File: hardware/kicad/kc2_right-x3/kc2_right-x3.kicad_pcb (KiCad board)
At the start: 2 copper layers, 194.8 x 133.8 mm, 98 parts, among them SW1 KEY_01, SW10 KEY_10, SW11 KEY_11, SW12 KEY_12, SW13 KEY_13, SW14 KEY_14, SW15 KEY_15, SW16 KEY_16, SW17 KEY_17, SW18 KEY_18, SW19 KEY_19, SW2 KEY_02, SW20 KEY_20, SW21 KEY_21, SW22 KEY_22, SW23 KEY_23, SW24 KEY_24, SW25 KEY_25, SW26 KEY_26, SW27 KEY_27, SW28 KEY_28, SW29 KEY_29, SW3 KEY_03, SW30 KEY_30, SW31 KEY_31, SW32 KEY_32, SW33 KEY_33, SW34 KEY_34, SW35 KEY_35, SW36 KEY_36, SW37 KEY_37, SW38 KEY_38, SW39 KEY_39, SW4 KEY_04, SW40 KEY_40, SW41 KEY_41, SW42 KEY_42, SW43 KEY_43, SW44 KEY_44, SW45 KEY_45, SW5 KEY_05, SW6 KEY_06, SW7 KEY_07, SW8 KEY_08, SW9 KEY_09, U1 nice!nano_v2_socket_24pin

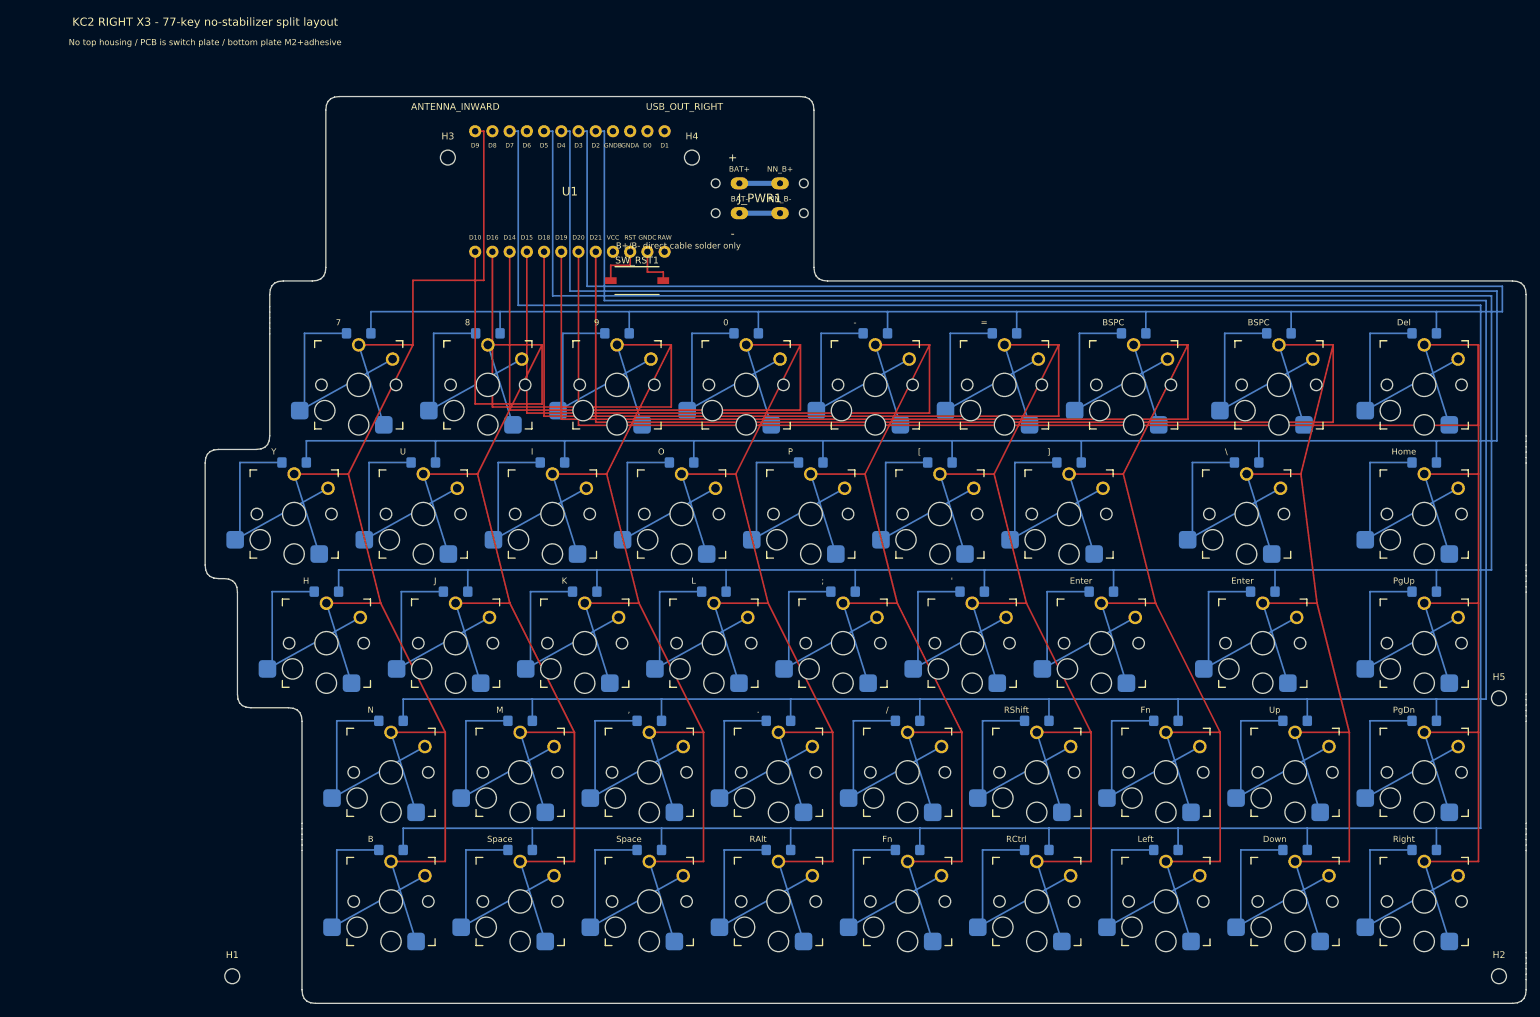
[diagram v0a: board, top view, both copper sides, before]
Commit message: fix: KC2 X3 발주 차단 해소
- nice!nano 좌/우 전용 풋프린트 추가 및 controller/switch/power 추적성 정리

- switch pad island routing, edge clearance, DRC error/warning 해소

- 좌/우 PCB, DSN/SES, Gerber/Excellon/fabrication zip/render/DRC JSON 갱신
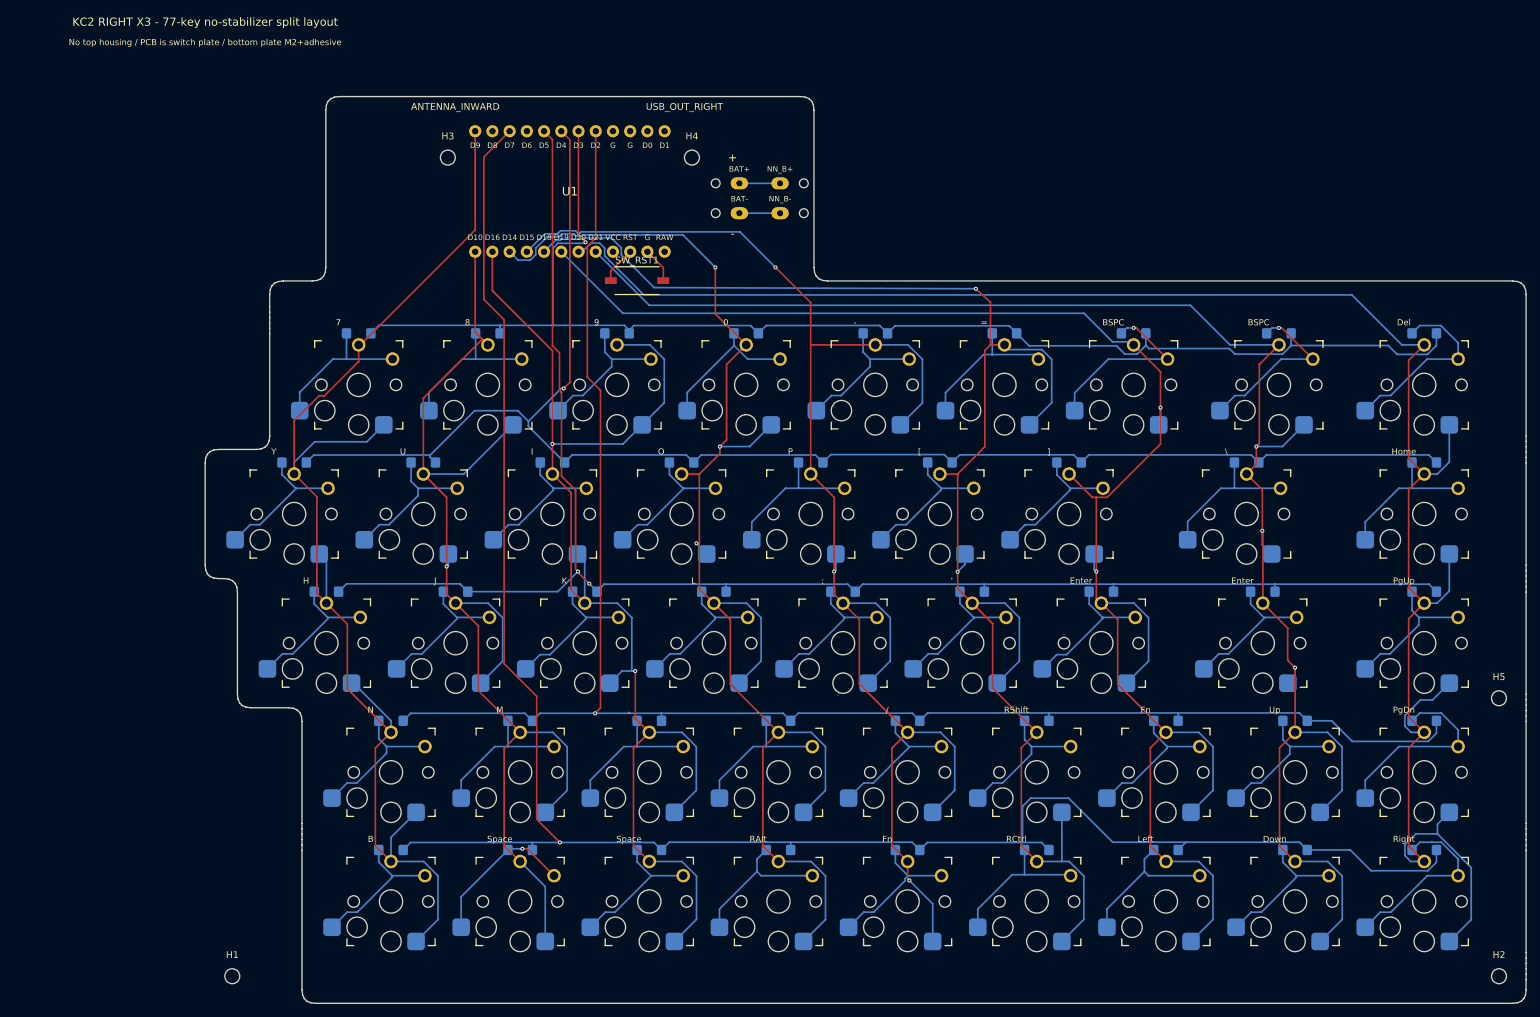
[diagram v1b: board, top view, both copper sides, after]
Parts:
- U1: footprint KC2:NiceNanoV2_Socket_24Pin -> KC2:NiceNanoV2_Socket_24Pin_USB_OUT_RIGHT
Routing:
- net R_ROW2: track 403.3 -> 238.7 mm, vias 0 -> 2
- net R_ROW1: track 388.1 -> 226.5 mm, vias 0 -> 1
- net R_ROW0: track 358.6 -> 204.9 mm, vias 0 -> 1
- net R_ROW3: track 403.6 -> 250.6 mm, vias 0 -> 1
- net R_ROW4: track 433.8 -> 286.7 mm, vias 0 -> 1
- net R_COL7: track 324.7 -> 242.2 mm, vias 0 -> 3
- net R_COL8: track 348.2 -> 282.5 mm
- net R_COL6: track 311.2 -> 246.3 mm, vias 0 -> 2
- net R_COL5: track 293.8 -> 233.9 mm, vias 0 -> 2
- net R_COL4: track 276.4 -> 220.3 mm, vias 0 -> 3
- net R_COL2: track 241.6 -> 187.2 mm, vias 0 -> 2
- net R_COL3: track 259.0 -> 205.2 mm, vias 0 -> 3
- net R_COL1: track 224.2 -> 172.2 mm, vias 0 -> 1
- net R_COL0: track 226.4 -> 189.6 mm
- net RK32_D: track 34.0 -> 21.6 mm
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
